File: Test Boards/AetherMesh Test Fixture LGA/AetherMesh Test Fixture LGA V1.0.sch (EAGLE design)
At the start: 5 parts, among them J1 POWER_JACKEJ508A, M1 AETHERMESH_MODULESMD_HOLES

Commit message: Updated test boards with silkscreen pin names and current measurment jumper
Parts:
- added JP3: (no value), 1. growflux:M02LOCK
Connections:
- new net N$3: JP2.10, JP3.1, M1.VCC
- net VCC: now also JP3.2; no longer JP2.10, M1.VCC

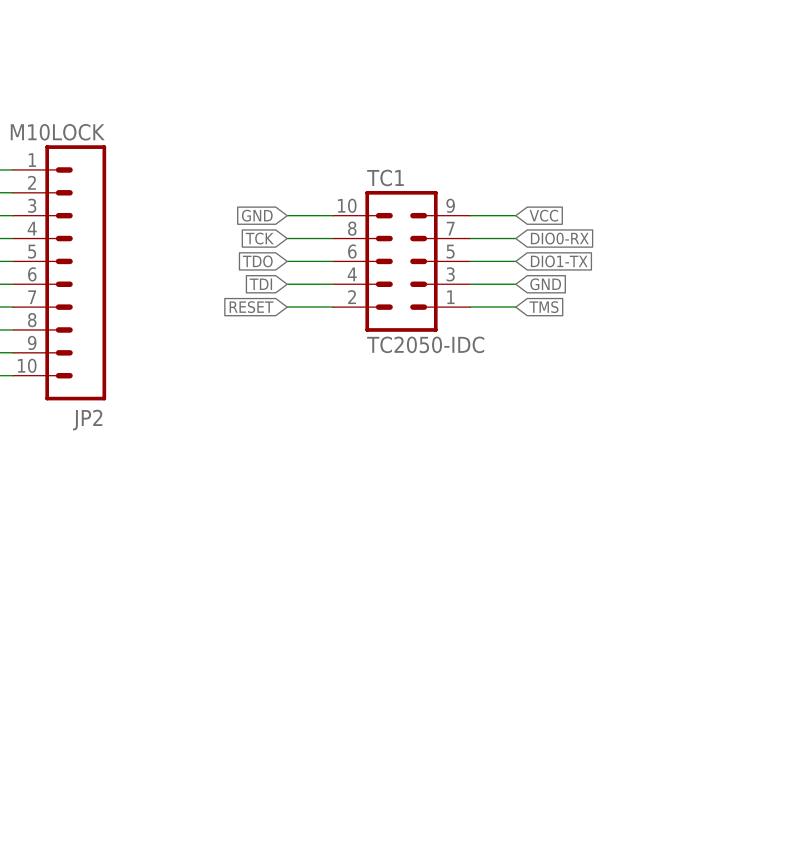
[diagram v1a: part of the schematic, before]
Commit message: Updated reference designs and test boards with latest XDS programmer tag connect header
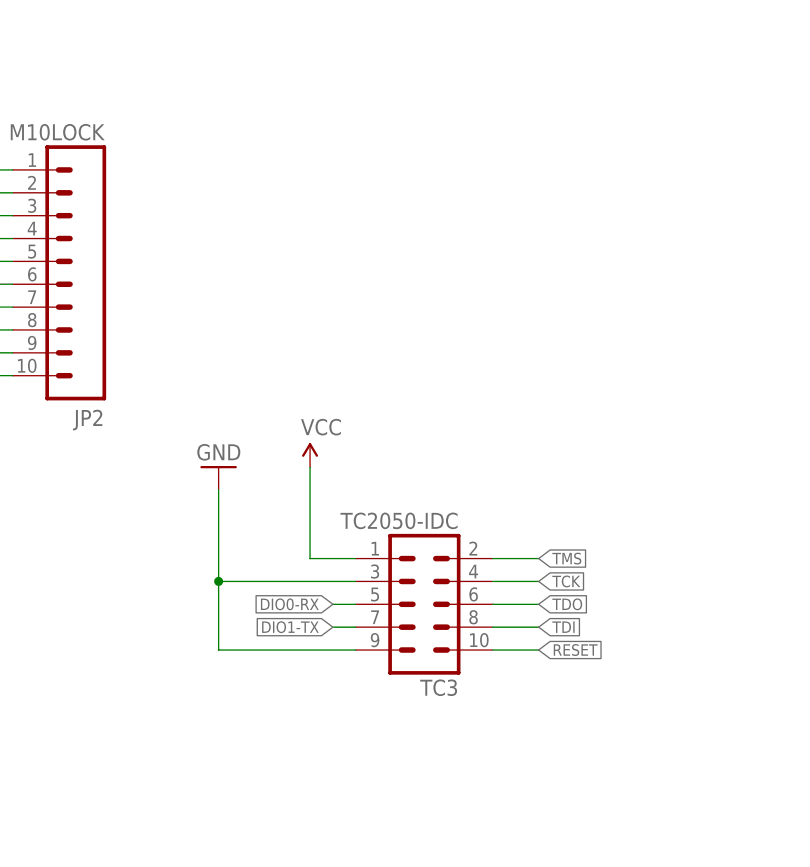
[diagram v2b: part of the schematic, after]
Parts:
- removed TC1: TC2050-IDC, TagConnect:TC2050-IDC
- added TC3: TC2050-IDC, TagConnect:TC2050-IDC
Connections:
- net DIO0-RX: now also TC3.5; no longer TC1.7
- net DIO1-TX: now also TC3.7; no longer TC1.5
- net GND: now also TC3.3, TC3.9; no longer TC1.10, TC1.3
- net RESET: now also TC3.10; no longer TC1.2
- net TCK: now also TC3.4; no longer TC1.8
- net TDI: now also TC3.8; no longer TC1.4
- net TDO: now also TC3.6; no longer TC1.6
- net TMS: now also TC3.2; no longer TC1.1
- net VCC: now also TC3.1; no longer TC1.9
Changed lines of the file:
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@@
 <?xml version="1.0" encoding="utf-8"?>
 <!DOCTYPE eagle SYSTEM "eagle.dtd">
-<eagle version="8.4.1">
+<eagle version="9.0.0">
 <drawing>
 <settings>
@@
 <layer number="59" name="tCarbon" color="7" fill="1" visible="no" active="no"/>
 <layer number="60" name="bCarbon" color="7" fill="1" visible="no" active="no"/>
+<layer number="88" name="SimResults" color="9" fill="1" visible="yes" active="yes"/>
+<layer number="89" name="SimProbes" color="9" fill="1" visible="yes" active="yes"/>
 <layer number="90" name="Modules" color="5" fill="1" visible="yes" active="yes"/>
 <layer number="91" name="Nets" color="2" fill="1" visible="yes" active="yes"/>
@@
 <part name="GND14" library="3. growflux" library_urn="urn:adsk.eagle:library:207379" deviceset="GND" device=""/>
 <part name="M1" library="AetherConnectivity" deviceset="AETHERMESH_MODULE" device="SMD_HOLES"/>
-<part name="TC1" library="TagConnect" deviceset="TC2050-IDC" device=""/>
 <part name="J1" library="3. growflux" deviceset="POWER_JACK" device="EJ508A"/>
 <part name="SUPPLY1" library="3. growflux" library_urn="urn:adsk.eagle:library:207379" deviceset="VCC" device=""/>
@@
 <part name="JP3" library="1. growflux" deviceset="M02" device="LOCK"/>
 <part name="SUPPLY2" library="3. growflux" library_urn="urn:adsk.eagle:library:207379" deviceset="VCC" device=""/>
+<part name="TC3" library="TagConnect" deviceset="TC2050-IDC" device=""/>
+<part name="GND2" library="SparkFun-Aesthetics" deviceset="GND" device=""/>
+<part name="SUPPLY3" library="3. growflux" library_urn="urn:adsk.eagle:library:207379" deviceset="VCC" device=""/>
 </parts>
 <sheets>
@@
 <instance part="GND14" gate="1" x="78.74" y="83.82"/>
 <instance part="M1" gate="G$1" x="93.98" y="88.9"/>
-<instance part="TC1" gate="A" x="198.12" y="104.14"/>
 <instance part="J1" gate="G$1" x="111.76" y="58.42"/>
 <instance part="SUPPLY1" gate="G$1" x="129.54" y="76.2"/>
@@
 <instance part="JP3" gate="G$1" x="134.62" y="124.46"/>
 <instance part="SUPPLY2" gate="G$1" x="149.86" y="132.08"/>
+<instance part="TC3" gate="A" x="200.66" y="66.04" rot="R180"/>
+<instance part="GND2" gate="1" x="177.8" y="81.28" rot="R180"/>
+<instance part="SUPPLY3" gate="G$1" x="187.96" y="81.28"/>
 </instances>
 <busses>
@@
 </segment>
 <segment>
-<pinref part="TC1" gate="A" pin="10"/>
-<wire x1="185.42" y1="109.22" x2="190.5" y2="109.22" width="0.1524" layer="91"/>
-<label x="185.42" y="109.22" size="1.27" layer="95" rot="R180" xref="yes"/>
-</segment>
-<segment>
-<pinref part="TC1" gate="A" pin="3"/>
-<wire x1="210.82" y1="101.6" x2="205.74" y2="101.6" width="0.1524" layer="91"/>
-<label x="210.82" y="101.6" size="1.27" layer="95" xref="yes"/>
-</segment>
-<segment>
 <pinref part="J1" gate="G$1" pin="GND"/>
 <pinref part="GND1" gate="1" pin="GND"/>
@@
 <wire x1="129.54" y1="60.96" x2="129.54" y2="53.34" width="0.1524" layer="91"/>
 </segment>
+<segment>
+<pinref part="TC3" gate="A" pin="3"/>
+<wire x1="193.04" y1="68.58" x2="177.8" y2="68.58" width="0.1524" layer="91"/>
+<wire x1="177.8" y1="68.58" x2="177.8" y2="78.74" width="0.1524" layer="91"/>
+<pinref part="GND2" gate="1" pin="GND"/>
+<junction x="177.8" y="68.58"/>
+<pinref part="TC3" gate="A" pin="9"/>
+<wire x1="193.04" y1="60.96" x2="177.8" y2="60.96" width="0.1524" layer="91"/>
+<wire x1="177.8" y1="60.96" x2="177.8" y2="68.58" width="0.1524" layer="91"/>
+</segment>
 </net>
 <net name="VCC" class="0">
-<segment>
-<pinref part="TC1" gate="A" pin="9"/>
-<wire x1="210.82" y1="109.22" x2="205.74" y2="109.22" width="0.1524" layer="91"/>
-<label x="210.82" y="109.22" size="1.27" layer="95" xref="yes"/>
-</segment>
 <segment>
 <pinref part="J1" gate="G$1" pin="PWR"/>
@@
 <wire x1="149.86" y1="127" x2="149.86" y2="132.08" width="0.1524" layer="91"/>
 </segment>
+<segment>
+<pinref part="TC3" gate="A" pin="1"/>
+<wire x1="187.96" y1="71.12" x2="193.04" y2="71.12" width="0.1524" layer="91"/>
+<pinref part="SUPPLY3" gate="G$1" pin="VCC"/>
+<wire x1="187.96" y1="81.28" x2="187.96" y2="71.12" width="0.1524" layer="91"/>
+</segment>
 </net>
 <net name="ENC_RESET" class="0">
@@
 </segment>
 <segment>
-<pinref part="TC1" gate="A" pin="1"/>
-<wire x1="210.82" y1="99.06" x2="205.74" y2="99.06" width="0.1524" layer="91"/>
-<label x="210.82" y="99.06" size="1.27" layer="95" xref="yes"/>
+<pinref part="TC3" gate="A" pin="2"/>
+<wire x1="213.36" y1="71.12" x2="208.28" y2="71.12" width="0.1524" layer="91"/>
+<label x="213.36" y="71.12" size="1.27" layer="95" xref="yes"/>
 </segment>
 </net>
@@
 </segment>
 <segment>
-<pinref part="TC1" gate="A" pin="8"/>
-<wire x1="185.42" y1="106.68" x2="190.5" y2="106.68" width="0.1524" layer="91"/>
-<label x="185.42" y="106.68" size="1.27" layer="95" rot="R180" xref="yes"/>
+<pinref part="TC3" gate="A" pin="4"/>
+<wire x1="213.36" y1="68.58" x2="208.28" y2="68.58" width="0.1524" layer="91"/>
+<label x="213.36" y="68.58" size="1.27" layer="95" xref="yes"/>
 </segment>
 </net>
@@
 </segment>
 <segment>
-<pinref part="TC1" gate="A" pin="6"/>
-<wire x1="185.42" y1="104.14" x2="190.5" y2="104.14" width="0.1524" layer="91"/>
-<label x="185.42" y="104.14" size="1.27" layer="95" rot="R180" xref="yes"/>
+<pinref part="TC3" gate="A" pin="6"/>
+<wire x1="213.36" y1="66.04" x2="208.28" y2="66.04" width="0.1524" layer="91"/>
+<label x="213.36" y="66.04" size="1.27" layer="95" xref="yes"/>
 </segment>
 </net>
@@
 </segment>
 <segment>
-<pinref part="TC1" gate="A" pin="4"/>
-<wire x1="185.42" y1="101.6" x2="190.5" y2="101.6" width="0.1524" layer="91"/>
-<label x="185.42" y="101.6" size="1.27" layer="95" rot="R180" xref="yes"/>
+<pinref part="TC3" gate="A" pin="8"/>
+<wire x1="213.36" y1="63.5" x2="208.28" y2="63.5" width="0.1524" layer="91"/>
+<label x="213.36" y="63.5" size="1.27" layer="95" xref="yes"/>
 </segment>
 </net>
@@
 </segment>
 <segment>
-<pinref part="TC1" gate="A" pin="2"/>
-<wire x1="185.42" y1="99.06" x2="190.5" y2="99.06" width="0.1524" layer="91"/>
-<label x="185.42" y="99.06" size="1.27" layer="95" rot="R180" xref="yes"/>
+<pinref part="TC3" gate="A" pin="10"/>
+<wire x1="208.28" y1="60.96" x2="213.36" y2="60.96" width="0.1524" layer="91"/>
+<label x="213.36" y="60.96" size="1.27" layer="95" xref="yes"/>
 </segment>
 </net>
@@
 </segment>
 <segment>
-<pinref part="TC1" gate="A" pin="5"/>
-<wire x1="210.82" y1="104.14" x2="205.74" y2="104.14" width="0.1524" layer="91"/>
-<label x="210.82" y="104.14" size="1.27" layer="95" xref="yes"/>
+<pinref part="TC3" gate="A" pin="7"/>
+<wire x1="190.5" y1="63.5" x2="193.04" y2="63.5" width="0.1524" layer="91"/>
+<label x="190.5" y="63.5" size="1.27" layer="95" rot="R180" xref="yes"/>
 </segment>
 </net>
@@
 </segment>
 <segment>
-<pinref part="TC1" gate="A" pin="7"/>
-<wire x1="210.82" y1="106.68" x2="205.74" y2="106.68" width="0.1524" layer="91"/>
-<label x="210.82" y="106.68" size="1.27" layer="95" xref="yes"/>
-</segment>
-</net>
+<pinref part="TC3" gate="A" pin="5"/>
+<wire x1="193.04" y1="66.04" x2="190.5" y2="66.04" width="0.1524" layer="91"/>
+<label x="190.5" y="66.04" size="1.27" layer="95" rot="R180" xref="yes"/>
+</segment>
+</net>
